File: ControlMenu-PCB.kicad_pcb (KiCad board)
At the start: 2 copper layers, 81.3 x 63 mm, 10 parts, among them J1 Conn_01x08, J2 Conn_01x04

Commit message: 5V to Ground Fixes
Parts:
- removed REF** (x4): MountingHole_3.2mm_M3_DIN965_Pad, MountingHole:MountingHole_3.2mm_M3_DIN965_Pad
- 100s1, 10s1, 1s1, Enter1: footprint RobsFoots:PB86-A-FP -> AA-ROB-FULL:PB86-A-FP
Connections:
- 100s1 pad 1: /5V -> /GND
- 10s1 pad 1: /5V -> /GND
- 1s1 pad 1: /5V -> /GND
- Enter1 pad 1: /5V -> /GND
- J1 pad 8: /5V -> Net-(J1-Pad8)
- J2 pad 1: /5V -> Net-(J1-Pad8)
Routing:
- net /5V: track 207.8 -> 0.00 mm
- net /GND: track 14.7 -> 79.1 mm
- net Net-(J1-Pad8): track 0.00 -> 42.9 mm
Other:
- board text added: "Control Menu PCB V0.1.2"
- board text added: "Control Menu V0.1.2"
- board text removed: "Control Menu PCB V0.1.0"
- board text removed: "Control Menu V0.1.0"

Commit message: autosync
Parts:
- added REF**: MountingHole_3.2mm_M3_DIN965_Pad, MountingHole:MountingHole_3.2mm_M3_DIN965_Pad, F.Cu at (192.1, 153.9)
- added REF**: MountingHole_3.2mm_M3_DIN965_Pad, MountingHole:MountingHole_3.2mm_M3_DIN965_Pad, F.Cu at (267.4, 96.9)
- added REF**: MountingHole_3.2mm_M3_DIN965_Pad, MountingHole:MountingHole_3.2mm_M3_DIN965_Pad, F.Cu at (192.1, 96.9)
- added REF**: MountingHole_3.2mm_M3_DIN965_Pad, MountingHole:MountingHole_3.2mm_M3_DIN965_Pad, F.Cu at (267.4, 153.9)
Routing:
- net /GND: track 79.1 -> 314.0 mm

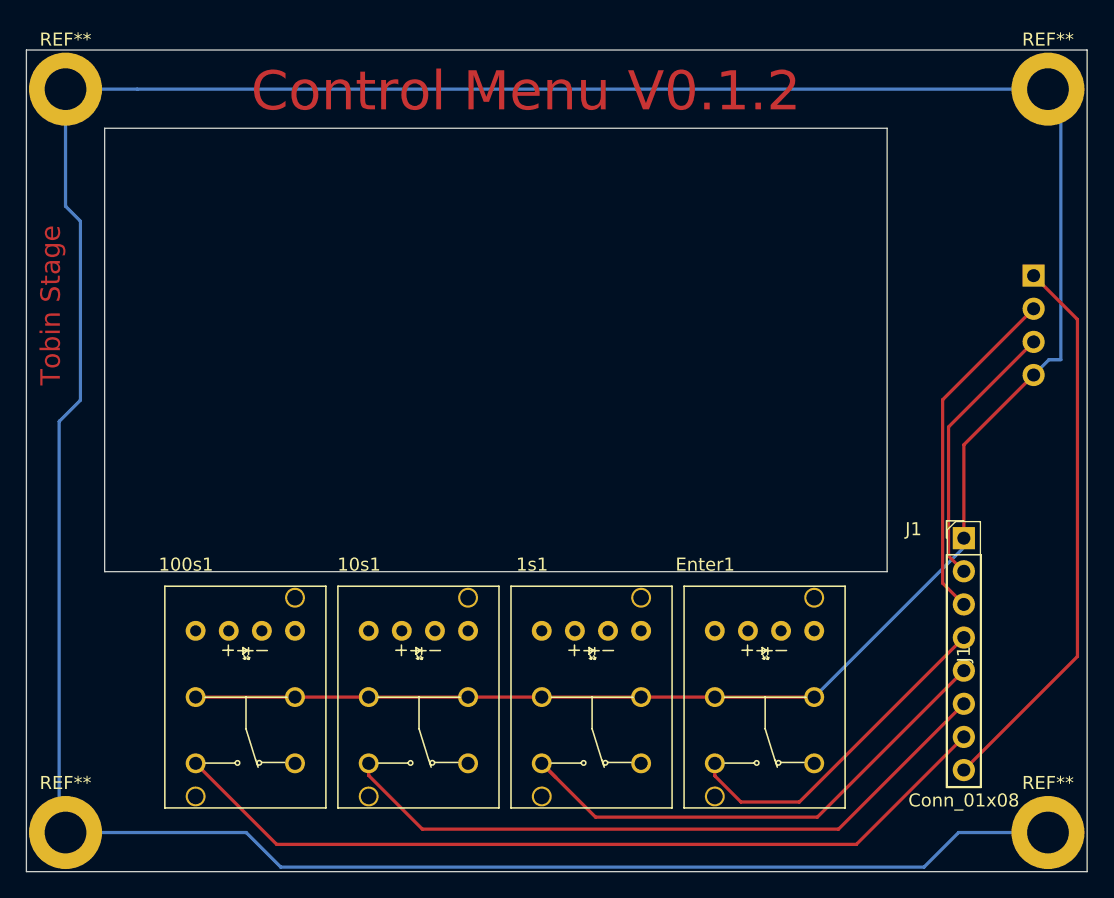
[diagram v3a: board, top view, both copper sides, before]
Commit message: Screen mount cutout reduced, I2C re-ordered.
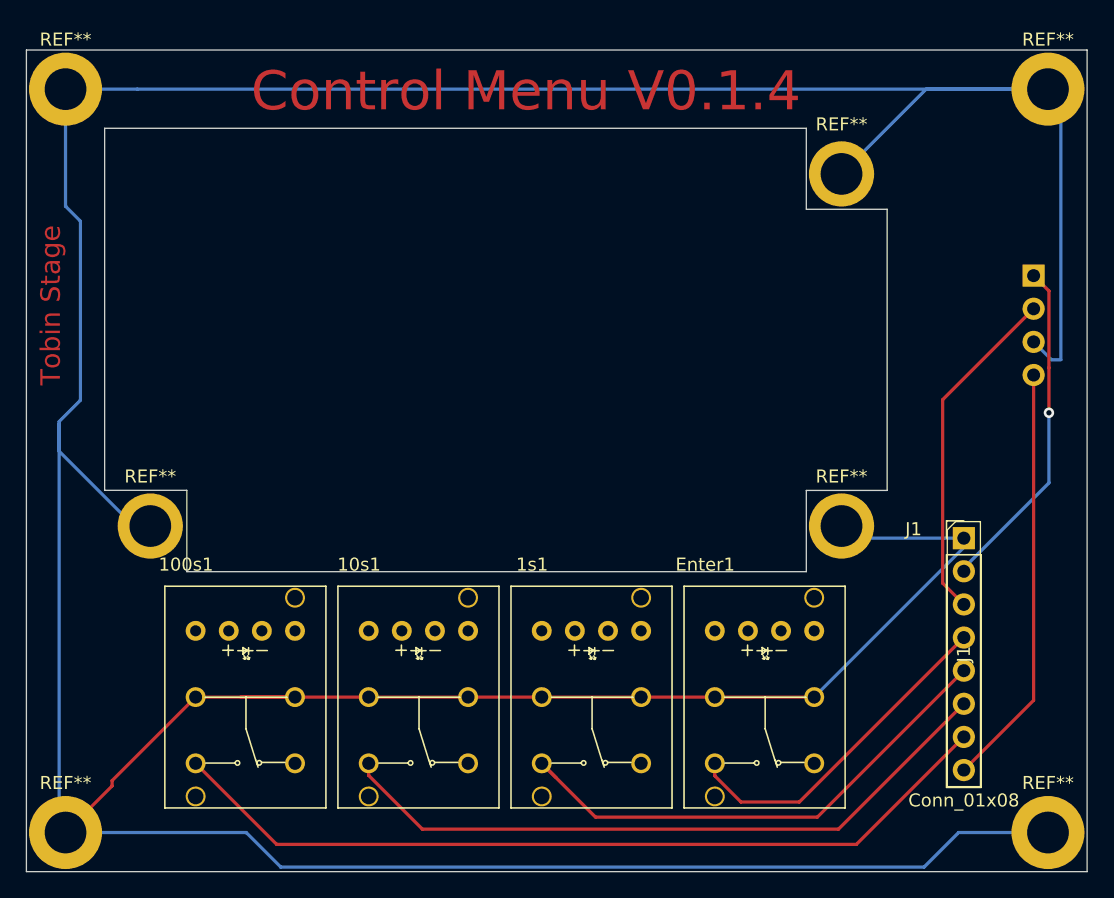
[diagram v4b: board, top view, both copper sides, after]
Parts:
- added REF**: MountingHole_3.2mm_M3_DIN965_Pad, MountingHole:MountingHole_3.2mm_M3_DIN965_Pad, F.Cu at (198.6, 130.4)
- added REF**: MountingHole_3.2mm_M3_DIN965_Pad, MountingHole:MountingHole_3.2mm_M3_DIN965_Pad, F.Cu at (251.6, 130.4)
- added REF**: MountingHole_3.2mm_M3_DIN965_Pad, MountingHole:MountingHole_3.2mm_M3_DIN965_Pad, F.Cu at (251.6, 103.4)
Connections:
- J2 pad 1: Net-(J1-Pad8) -> /SCL
- J2 pad 3: /SCL -> /GND
- J2 pad 4: /GND -> Net-(J1-Pad8)
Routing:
- net /GND: track 314.0 -> 357.8 mm
- net Net-(J1-Pad8): track 42.9 -> 32.5 mm
- net /SCL: track 20.8 -> 25.9 mm, vias 0 -> 1
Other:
- outline, holes or cut-outs redrawn
- board text added: "Control Menu PCB V0.1.4"
- board text added: "Control Menu V0.1.4"
- board text removed: "Control Menu PCB V0.1.2"
- board text removed: "Control Menu V0.1.2"
